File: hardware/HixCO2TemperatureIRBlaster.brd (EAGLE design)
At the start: 17 x 12.8 mm, 33 parts, among them J1 FTDI, J2 IEC320C8, J3 XH4P, Q1 AO3400, Q2 AO3400, U1 ESP12E, U2 LM3940, U3 HLK-PM01, U4 DS18B20

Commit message: update hardware
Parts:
- removed C3: 100nF, resistor:C1206
- removed R1, R3, R4: 10K, rcl:R1206
- removed R13: 2.2K, rcl:R1206
- removed S1: PROG, 0_HixField:SMDPUSHBTN_TYPE1
- removed S2: RST, 0_HixField:SMDPUSHBTN_TYPE1
- removed U1: ESP12E, 0_HixField:ESP8266(ESP12E)
- added C5: 100nF, resistor:C1206
- added R10, R11, R15: 10K, rcl:R1206
- added R12: 2.2K, rcl:R1206
- added S3: RST, 0_HixField:SMDPUSHBTN_TYPE1
- added S4: PROG, 0_HixField:SMDPUSHBTN_TYPE1
- added U$1: MHZ-19_CO2, 0_HixField:MHZ-19_CO2
- added U$2: ESP8266(ESP12E)V2, 0_HixField:ESP8266(ESP12E)
- C1, C2: device resistor:C1206 -> rcl:SMC_A
- C6: device resistor:E3,5-8 -> 0_HixField:ELKO_6.3X12_FLAT
- IRLED1, IRLED2, IRLED3: value (none) -> LEDLED5MM_ANGLED1; device led:LED5MM -> 0_HixField:LED5MM_ANGLED1
- R8, R9: device resistor:R1206 -> rcl:R1206
- moved U3 198.9 mm to (-76.2, -231.1)
- moved R14 195.2 mm to (-99.1, -238.8)
- moved C1 185.3 mm to (-61.0, -246.4), turned to 270 degrees
- moved F1 183.8 mm to (-99.1, -223.5), turned to 90 degrees
- moved U2 173.6 mm to (-55.9, -246.4)
- moved J2 170.6 mm to (-109.2, -231.1), turned to 90 degrees
- moved C6 169.4 mm to (-53.3, -226.1), turned to 90 degrees
- moved C2 163.9 mm to (-50.8, -246.4), turned to 90 degrees
- moved R2 145.8 mm to (-53.3, -294.6)
- moved B1 139.0 mm to (-111.8, -256.5)
- moved J1 124.6 mm to (-91.4, -254.0), turned to 270 degrees
- moved U4 80.3 mm to (-71.1, -259.1)
- moved R9 74.7 mm to (-58.4, -259.1)
- moved R7 61.4 mm to (-58.4, -269.2)
- moved Q1 60.6 mm to (-58.4, -276.9)
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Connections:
- removed net ENABLE: R3.1, U1.CH_PD
- removed net GPIO0: R2.1, S1.1, U1.GPIO0
- removed net GPIO15: R4.2, U1.GPIO15
- removed net RESET: R1.1, S2.1, U1.RESET
- new net N$10: R2.2, U$2.GPIO15_CS_TXD2
- new net N$11: U$2.GPIO16_WAKE
- new net N$7: R10.1, S3.1, U$2.RST
- new net N$8: R11.1, U$2.ENABLE
- new net N$9: R15.1, S4.1, U$2.GPIO0_FLASH
- new net VIN: U$1.VIN
- new net VO: U$1.VO
- net 3.3V: now also C2.+, C5.1, J3.2, R10.2, R11.2, R12.2, R15.2, U$2.VCC; no longer C2.1, C3.1, R1.2, R13.2, R2.2, R3.2, U1.VCC
- net 5.0V: now also C1.+; no longer C1.1, J3.2
- net AC2: now also J2.AC1; no longer J2.P$1
- net BEEP: now also R12.1, U$2.GPIO2_TXD1; no longer R13.1, U1.GPIO2
- net GND: now also C1.-, C2.-, C5.2, R2.1, S3.2, S4.2, U$1.GND, U$2.GND; no longer C1.2, C2.2, C3.2, R4.1, S1.2, S2.2, U1.GND
- net IR_IN: now also U$2.GPIO14_SCLK; no longer U1.GPIO14
- net IR_OUT: now also U$2.GPIO13_MOSI; no longer U1.GPIO13
- net N$2: now also J2.AC2; no longer J2.P$2
- net N$3: now also IRLED1.CATHODE, IRLED2.CATHODE, IRLED3.CATHODE; no longer IRLED1.K, IRLED2.K, IRLED3.K
- net N$4: now also IRLED1.ANODE, IRLED2.ANODE, IRLED3.ANODE; no longer IRLED1.A, IRLED2.A, IRLED3.A
- net RXD: now also U$2.GPIO1_TXD0; no longer U1.TXD0
- net SCL: now also U$2.GPIO5_SCL; no longer U1.GPIO5
- net SDA: now also U$2.GPIO4_SDA; no longer U1.GPIO4
- net TEMP: now also U$2.GPIO12_MISO; no longer U1.GPIO12
- net TXD: now also U$2.GPIO3_RXD0; no longer U1.RXD0
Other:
- board size 17 x 12.8 mm -> 119.4 x 94 mm

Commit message: continued working on hardware models
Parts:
- C4, C5: device resistor:C1206 -> rcl:C1206
- C6: device 0_HixField:ELKO_6.3X12_FLAT -> 0_HixField:ELKO_RADIAL_STRAIGHT_4P_8D_9H
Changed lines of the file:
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@@
 </layers>
 <board>
-<fusionsync huburn="a.cGVyc29uYWw6dWUyZDExMjg2" projecturn="a.cGVyc29uYWw6dWUyZDExMjg2IzIwMjAwMzAyMjcwOTIxNDc2" f3durn="urn:adsk.wipprod:dm.lineage:z12vyTSqTrmJ0d_rSbxTSQ" pcbguid="cee08d37-9484-4f0e-931e-9f2835db71cd" lastpulledtime="" lastsyncedchangeguid="ced85851-942d-40e7-a919-b9f981cb1121"/>
+<fusionsync huburn="a.cGVyc29uYWw6dWUyZDExMjg2" projecturn="a.cGVyc29uYWw6dWUyZDExMjg2IzIwMjAwMzAyMjcwOTIxNDc2" f3durn="urn:adsk.wipprod:dm.lineage:z12vyTSqTrmJ0d_rSbxTSQ" pcbguid="cee08d37-9484-4f0e-931e-9f2835db71cd" lastpulledtime="" lastsyncedchangeguid="6cb196cf-ba27-88e1-32af-03c218abb9e6"/>
 <plain>
 <wire x1="-134.62" y1="-218.44" x2="-134.62" y2="-312.42" width="0.1524" layer="20"/>
@@
 <attribute name="VALUE" x="-95.123" y="-239.268" size="1.27" layer="27" ratio="10" rot="R90" align="center"/>
 </element>
-<element name="C6" library="0_HixField" library_urn="urn:adsk.eagle:library:13392178" package="ELKO_6.3X12_FLAT" package3d_urn="urn:adsk.eagle:package:13392182/1" value="680μF/6.3V" x="-53.34" y="-226.06" smashed="yes" rot="R90">
+<element name="C6" library="0_HixField" library_urn="urn:adsk.eagle:library:13392178" package="ELKO_RADIAL_STRAIGHT_4P_8D_9H" package3d_urn="urn:adsk.eagle:package:17790431/3" value="680μF/6.3V" x="-53.34" y="-226.06" smashed="yes" rot="R90">
 <attribute name="NAME" x="-56.134" y="-222.758" size="1.27" layer="25" ratio="10" rot="R90"/>
 <attribute name="VALUE" x="-50.292" y="-228.346" size="1.27" layer="27" ratio="10" rot="R90"/>
 </element>
 <element name="J2" library="0_HixField" library_urn="urn:adsk.eagle:library:13392178" package="IEC320C8" package3d_urn="urn:adsk.eagle:package:17723124/3" value="IEC320C8" x="-109.22" y="-231.14" smashed="yes" rot="R90"/>
-<element name="J1" library="0_HixField" package="FTDI" value="FTDI" x="-91.44" y="-254" smashed="yes" rot="R270">
+<element name="J1" library="0_HixField" library_urn="urn:adsk.eagle:library:13392178" package="FTDI" package3d_urn="urn:adsk.eagle:package:12836035/3" value="FTDI" x="-91.44" y="-254" smashed="yes" rot="R270">
 <attribute name="NAME" x="-87.63" y="-252.095" size="1.016" layer="25" align="center"/>
 </element>
-<element name="B1" library="0_HixField" package="BUZZER(12MM)" value="BUZZER(12MM)" x="-111.76" y="-256.54" smashed="yes">
+<element name="B1" library="0_HixField" library_urn="urn:adsk.eagle:library:13392178" package="BUZZER(12MM)" package3d_urn="urn:adsk.eagle:package:12836039/1" value="BUZZER(12MM)" x="-111.76" y="-256.54" smashed="yes">
 <attribute name="NAME" x="-111.76" y="-254" size="1.27" layer="25" align="center"/>
 <attribute name="VALUE" x="-111.76" y="-259.08" size="1.27" layer="27" align="center"/>
@@
 <attribute name="VALUE" x="-44.45" y="-297.18" size="1.27" layer="27"/>
 </element>
-<element name="C4" library="resistor" package="C1206" value="4.7μF" x="-43.18" y="-302.26" smashed="yes">
+<element name="C4" library="rcl" library_urn="urn:adsk.eagle:library:334" package="C1206" package3d_urn="urn:adsk.eagle:package:23618/2" value="4.7μF" x="-43.18" y="-302.26" smashed="yes">
 <attribute name="NAME" x="-44.45" y="-300.99" size="1.27" layer="25"/>
+<attribute name="POPULARITY" value="54" x="-43.18" y="-302.26" size="1.778" layer="27" display="off"/>
+<attribute name="SPICEPREFIX" value="C" x="-43.18" y="-302.26" size="1.778" layer="27" display="off"/>
 <attribute name="VALUE" x="-44.45" y="-304.8" size="1.27" layer="27"/>
 </element>
@@
 <attribute name="VALUE" x="-103.67" y="-274.4" size="1.4224" layer="27" rot="R90" align="center"/>
 </element>
-<element name="C5" library="resistor" package="C1206" value="100nF" x="-68.58" y="-294.64" smashed="yes">
+<element name="C5" library="rcl" library_urn="urn:adsk.eagle:library:334" package="C1206" package3d_urn="urn:adsk.eagle:package:23618/2" value="100nF" x="-68.58" y="-294.64" smashed="yes">
 <attribute name="NAME" x="-69.85" y="-293.37" size="1.27" layer="25"/>
+<attribute name="POPULARITY" value="54" x="-68.58" y="-294.64" size="1.778" layer="27" display="off"/>
+<attribute name="SPICEPREFIX" value="C" x="-68.58" y="-294.64" size="1.778" layer="27" display="off"/>
 <attribute name="VALUE" x="-69.85" y="-297.18" size="1.27" layer="27"/>
 </element>
@@
 <wire x1="-34.61" y1="-242.4" x2="-50.8" y2="-244.88" width="0" layer="19" extent="1-1"/>
 <wire x1="-43.18" y1="-264.16" x2="-59.842" y2="-269.24" width="0" layer="19" extent="1-1"/>
-<wire x1="-53.34" y1="-224.79" x2="-55.88" y2="-243.33" width="0" layer="19" extent="1-1"/>
-<wire x1="-61.5" y1="-223.44" x2="-53.34" y2="-224.79" width="0" layer="19" extent="1-1"/>
+<wire x1="-53.34" y1="-223.52" x2="-55.88" y2="-243.33" width="0" layer="19" extent="1-1"/>
+<wire x1="-61.5" y1="-223.44" x2="-53.34" y2="-223.52" width="0" layer="19" extent="1-1"/>
 <wire x1="-22.86" y1="-285.75" x2="-41.78" y2="-302.26" width="0" layer="19" extent="1-1"/>
 </signal>

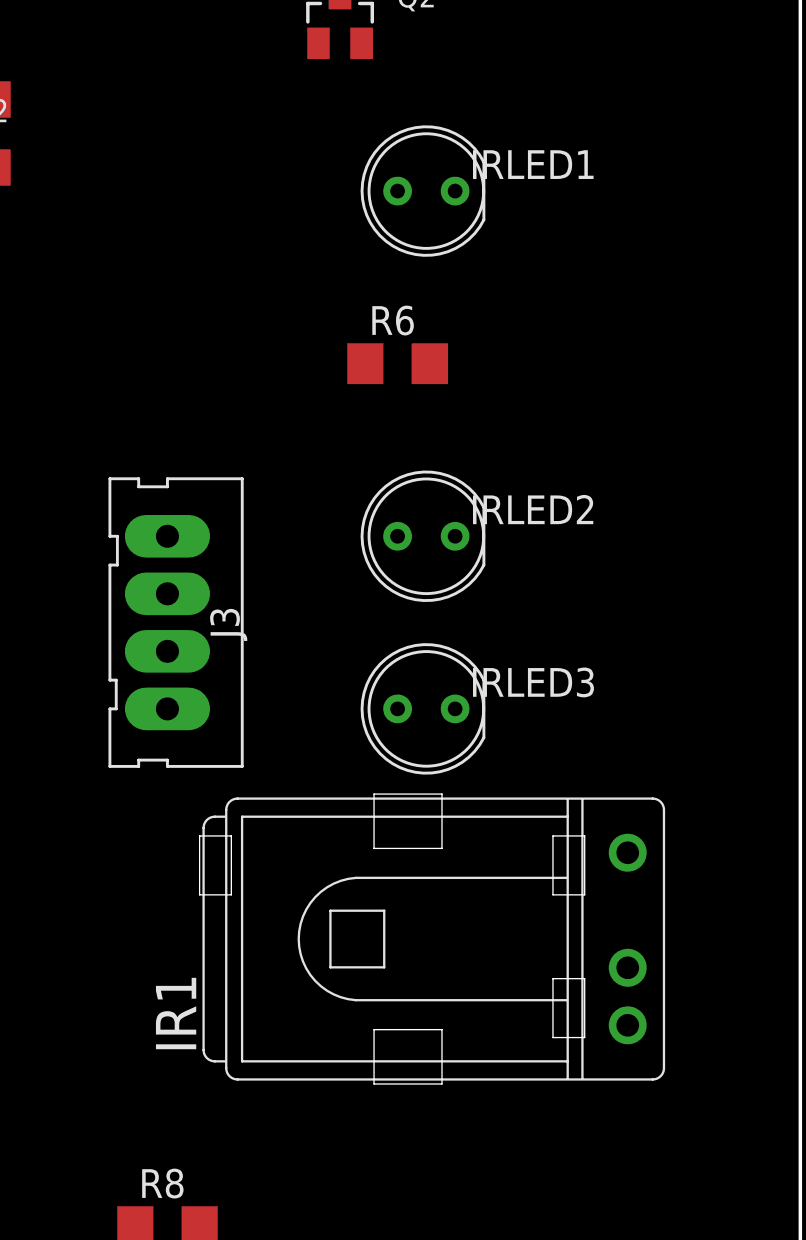
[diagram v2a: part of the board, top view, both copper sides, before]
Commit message: updated esp pin mapping
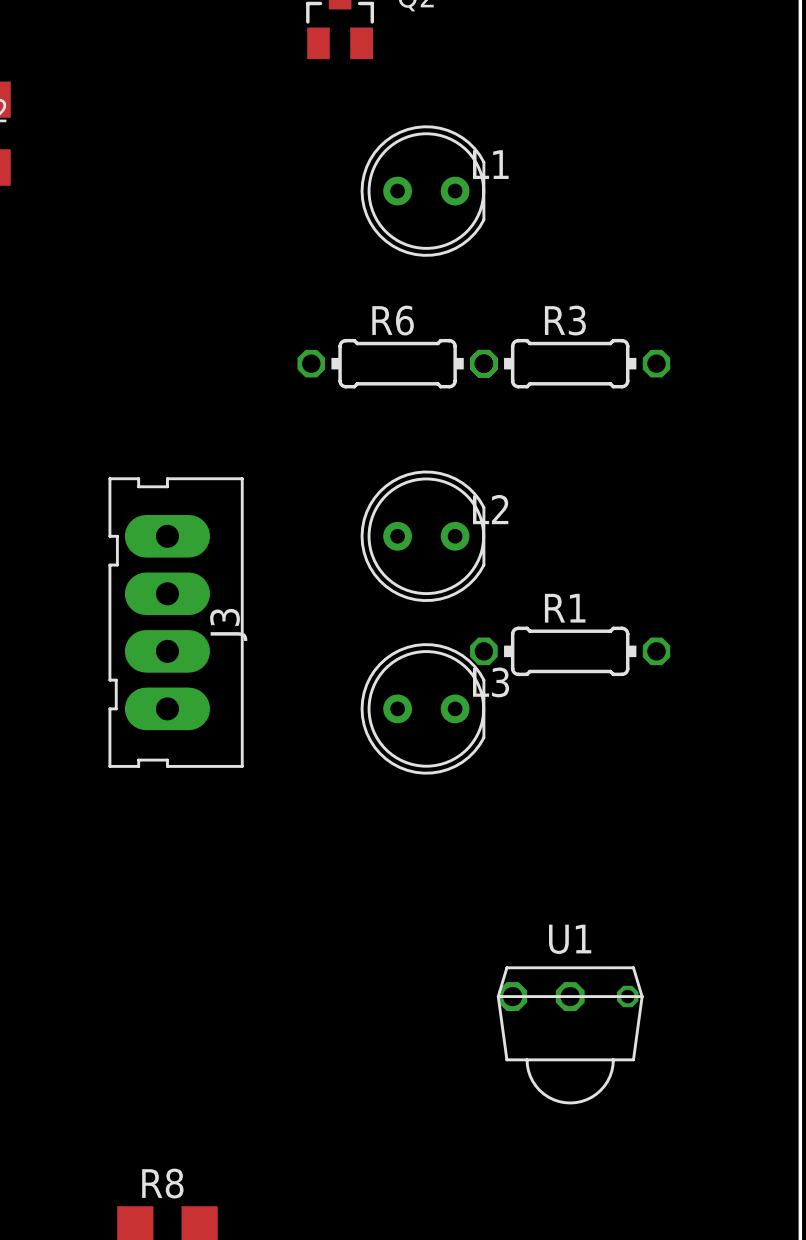
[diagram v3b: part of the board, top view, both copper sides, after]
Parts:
- removed IR1: TSOP1738TB1, telefunken:TSOP17_TB1
- added R1, R3: 68, rcl:0204/7
- added U1: TSOP2238, 0_HixField:TSOP2238
- R6: device rcl:R1206 -> rcl:0204/7
- renumbered IRLED1 to L1, IRLED2 to L2, IRLED3 to L3
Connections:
- net N$9 renamed RGB
- removed net N$11: U$2.GPIO16_WAKE
- removed net VIN: U$1.VIN
- new net CO2_RX: U$1.TX, U$2.GPIO13_MOSI
- new net CO2_TX: U$1.RX, U$2.GPIO16_WAKE
- new net N$9: L1.ANODE, R3.1
- net 5.0V: now also R1.2, R3.2, U$1.VIN
- net GND: now also U1.VCC; no longer IR1.GND
- net IR_IN: now also U$2.GPIO12_MISO, U1.OUT; no longer IR1.VO, U$2.GPIO14_SCLK
- net IR_OUT: now also R2.2, U$2.GPIO15_CS_TXD2; no longer U$2.GPIO13_MOSI
- net N$10: now also L3.ANODE, R1.1; no longer R2.2, U$2.GPIO15_CS_TXD2
- net N$4: no longer L1.ANODE, L3.ANODE
- net N$6: now also U1.GND; no longer IR1.VS
- net TEMP: now also U$2.GPIO14_SCLK; no longer U$2.GPIO12_MISO

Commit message: electronic hardware v1 complete
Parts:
- added C3: 100nF, rcl:C1206
- added U$3: LED_RGB, 0_HixField:LED_PL9823-F5
- F1: value 800mA -> 800mA 250V
- moved U1 108.2 mm to (-129.5, -264.2), turned to 270 degrees
- moved C4 95.4 mm to (-129.5, -261.6), turned to 90 degrees
- moved R8 90.1 mm to (-127.0, -261.6), turned to 90 degrees
- moved R11 79.5 mm to (-55.9, -227.3), flipped to the bottom, turned to 180 degrees
- moved R10 77.1 mm to (-55.9, -231.1), flipped to the bottom
- moved C5 71.5 mm to (-76.2, -223.5), flipped to the bottom
- moved R6 71.1 mm to (-95.2, -222.2), turned to 180 degrees
- moved R15 71.0 mm to (-55.9, -234.9), flipped to the bottom, turned to 180 degrees
- moved R9 69.0 mm to (-127.0, -251.5), turned to 270 degrees
- moved L2 68.8 mm to (-87.6, -222.2)
- moved R12 63.6 mm to (-63.5, -231.1), flipped to the bottom
- moved U$2 61.5 mm to (-59.7, -231.8), turned to 270 degrees
- moved U4 61.4 mm to (-132.1, -251.5), turned to 270 degrees
- moved R2 60.5 mm to (-63.5, -234.9), flipped to the bottom, turned to 180 degrees
- moved L3 52.5 mm to (-85.1, -265.4), turned to 180 degrees
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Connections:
- net 5.0V: now also C3.1, U$3.VCC
- net GND: now also C3.2, U$3.GND
- net RGB: now also U$3.DIN
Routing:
- net GND: track 0.00 -> 272.3 mm
- net 5.0V: track 0.00 -> 171.9 mm, vias 0 -> 1
- net 3.3V: track 0.00 -> 163.2 mm, vias 0 -> 1
- net N$3: track 0.00 -> 107.9 mm, vias 0 -> 1
- net TEMP: track 0.00 -> 87.1 mm, vias 0 -> 2
- net IR_IN: track 0.00 -> 83.7 mm, vias 0 -> 4
- net RGB: track 0.00 -> 72.4 mm, vias 0 -> 2
- net CO2_TX: track 0.00 -> 53.8 mm, vias 0 -> 2
- net CO2_RX: track 0.00 -> 53.0 mm
- net IR_OUT: track 0.00 -> 40.6 mm, vias 0 -> 2
- net BEEP: track 0.00 -> 36.1 mm, vias 0 -> 3
- net N$7: track 0.00 -> 31.7 mm, vias 0 -> 3
- net SCL: track 0.00 -> 28.3 mm
- net RXD: track 0.00 -> 26.5 mm
- net SDA: track 0.00 -> 26.3 mm
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- added copper zone on layer 16, net 3.3V
- added copper zone on layer 16, net 5.0V
- added copper zone on layer 1, net GND
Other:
- board size 119.4 x 94 mm -> 88.9 x 45.7 mm
